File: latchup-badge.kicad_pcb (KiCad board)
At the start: 2 copper layers, 101.6 x 71.1 mm, 39 parts, among them J1 USB_B_Micro, J2 CONN_02X06, J3 CONN_02X06, J4 CONN_02X05, U1 ICE40UP5K-SG48ITR, U2 TLV70012_SOT23-5, U3 TLV70033_SOT23-5, U4 M25PX32-VMW, X1 ASE-12.000MHz

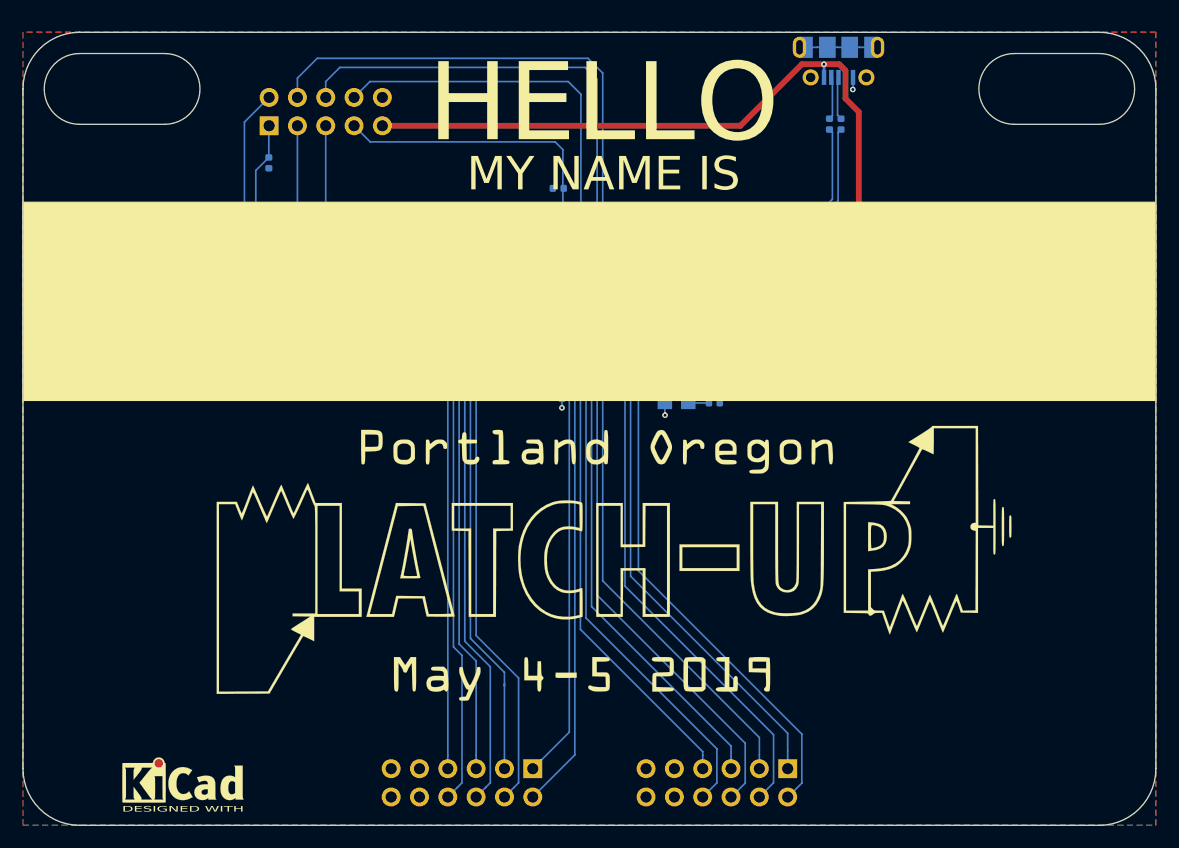
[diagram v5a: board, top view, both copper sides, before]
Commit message: Add RGB and a few buttons
Ready final review.

Signed-off-by: Michael Welling <mwelling@ieee.org>
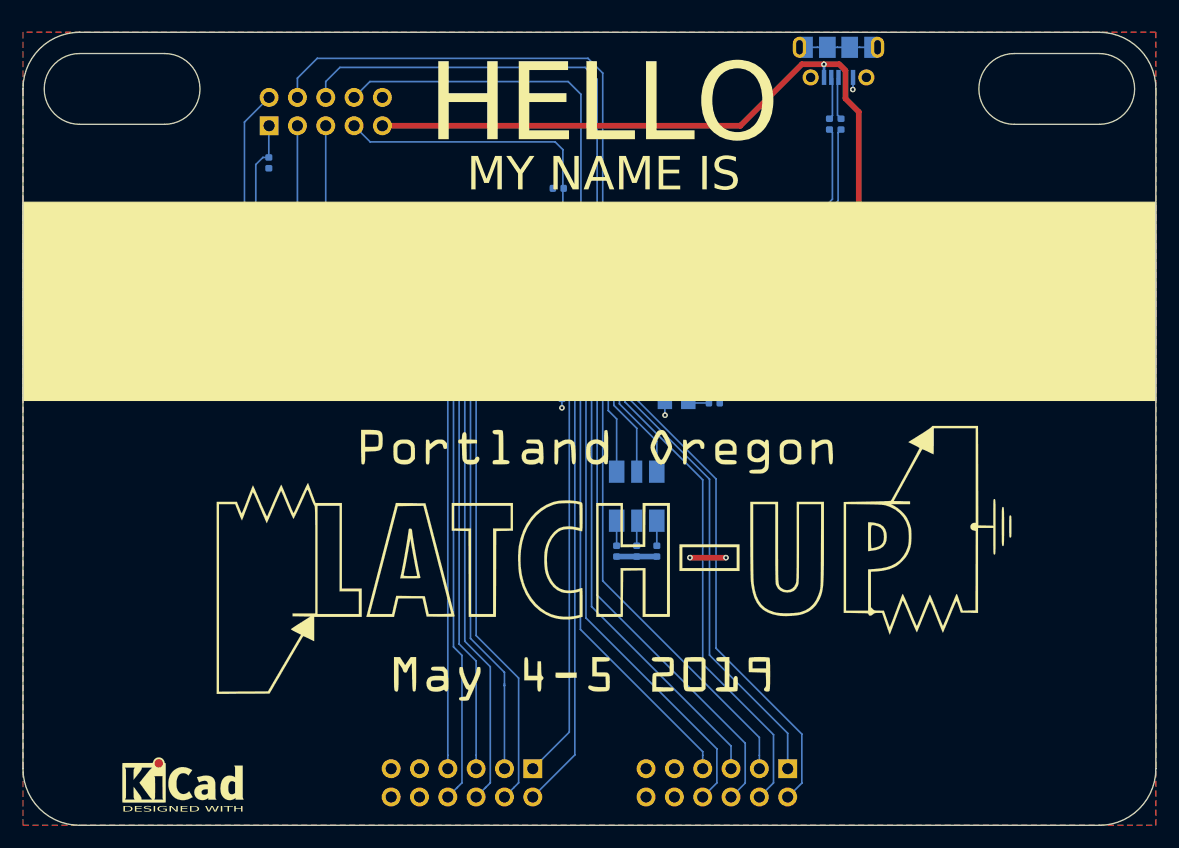
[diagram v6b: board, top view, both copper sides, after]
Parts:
- added D2: LED_RGB, latchup-badge:LED_RGB_PLLC-6, B.Cu at (131.2, 92.4)
- added R10: 330, Resistor_SMD:R_0402_1005Metric, B.Cu at (133.0, 97.3)
- added R11: 330, Resistor_SMD:R_0402_1005Metric, B.Cu at (131.2, 97.3)
- added R12: 330, Resistor_SMD:R_0402_1005Metric, B.Cu at (129.4, 97.3)
- added R13: 10K, Resistor_SMD:R_0402_1005Metric, B.Cu at (156.4, 71.7)
- added R14: 10K, Resistor_SMD:R_0402_1005Metric, B.Cu at (167.9, 71.7)
- added SW1: SW_Push, Button_Switch_SMD:SW_SPST_EVQQ2, B.Cu at (159.8, 75.8)
- added SW2: SW_Push, Button_Switch_SMD:SW_SPST_EVQQ2, B.Cu at (171.4, 75.8)
- moved G*** 17.3 mm to (93.9, 90.3), turned to 90 degrees
- moved C6 0.28 mm to (130.1, 71.4)
- moved D1 0.28 mm to (131.6, 71.4)
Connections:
- R8 pad 1: Net-(R8-Pad1) -> /FLASH_IO3_HLD
- R9 pad 1: Net-(R9-Pad1) -> /FLASH_IO2_WP
- U1 pad 20: Net-(U1-Pad20) -> /FLASH_IO3_HLD
- U1 pad 21: Net-(U1-Pad21) -> /FLASH_IO2_WP
- U1 pad 23: Net-(U1-Pad23) -> /BTN_B
- U1 pad 25: Net-(U1-Pad25) -> /BTN_A
- U1 pad 39: Net-(U1-Pad39) -> /RGB_BLUE
- U1 pad 40: Net-(U1-Pad40) -> /RGB_GREEN
- U1 pad 41: Net-(U1-Pad41) -> /RGB_RED
- U4 pad 3: Net-(R9-Pad1) -> /FLASH_IO2_WP
- U4 pad 7: Net-(R8-Pad1) -> /FLASH_IO3_HLD
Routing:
- net /BTN_A: track 0.00 -> 48.9 mm, vias 0 -> 2
- net /BTN_B: track 0.00 -> 37.8 mm, vias 0 -> 2
- net /FLASH_IO3_HLD: track 0.00 -> 20.2 mm, vias 0 -> 2
- net /FLASH_IO2_WP: track 0.00 -> 10.3 mm, vias 0 -> 2
- net /RGB_BLUE: track 0.00 -> 10.2 mm
- net /RGB_GREEN: track 0.00 -> 9.62 mm
- net /RGB_RED: track 0.00 -> 9.08 mm
- net GND: track 25.6 -> 34.3 mm, vias 25 -> 29
- net +3V3: track 11.7 -> 18.6 mm, vias 2 -> 4
- net Net-(R8-Pad1): track 2.61 -> 0.00 mm
- net Net-(D?1555707827-Pad6): track 0.00 -> 2.24 mm
- net Net-(D?1555707827-Pad4): track 0.00 -> 2.24 mm
- net Net-(D?1555707827-Pad5): track 0.00 -> 2.24 mm
- net Net-(R9-Pad1): track 2.15 -> 0.00 mm
- net +5V: track 80.2 -> 81.4 mm, vias 5 -> 2

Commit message: See everyone at Latchup!
This is puppy is going to the fab.

Signed-off-by: Michael Welling <mwelling@ieee.org>
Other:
- board text added: "A"
- board text added: "B"

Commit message: Update to Kicad 6
Signed-off-by: Michael Welling <mwelling@ieee.org>
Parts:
- removed G***: LOGO, latchup-badge:logo_3
- removed G***: KiCad Logo, latchup-badge:KiCad-Logo_Copper_11mmx5mm
- removed G***: LOGO, latchup-badge:logo_2
- removed G***: LOGO, latchup-badge:logo_1
- removed G***: LOGO, latchup-badge:logo
- J2, J3: value CONN_02X06 -> Connector_Generic:Conn_02x06_Odd_Even
- J4: value CONN_02X05 -> Connector_Generic:Conn_02x05_Odd_Even
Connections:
- J1 pad 4: Net-(J1-Pad4) -> unconnected-(J1-Pad4)
- U1 pad 2: Net-(U1-Pad2) -> unconnected-(U1-Pad2)
- U1 pad 3: Net-(U1-Pad3) -> unconnected-(U1-Pad3)
- U1 pad 31: Net-(U1-Pad31) -> unconnected-(U1-Pad31)
- U1 pad 32: Net-(U1-Pad32) -> unconnected-(U1-Pad32)
- U1 pad 34: Net-(U1-Pad34) -> unconnected-(U1-Pad34)
- U1 pad 4: Net-(U1-Pad4) -> unconnected-(U1-Pad4)
- U2 pad 4: Net-(U2-Pad4) -> unconnected-(U2-Pad4)
- U3 pad 4: Net-(U3-Pad4) -> unconnected-(U3-Pad4)
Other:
- net class Default removed
